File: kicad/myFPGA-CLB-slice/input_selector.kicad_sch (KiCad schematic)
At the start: 26 parts, among them U1 74AHCT595, U32 74LS153, U33 74LS153, U34 74LS153, U35 74LS153

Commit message: fixed kicad names, updated architecure, started CBv
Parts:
- added R12, R13, R14, R15, R16, R17, R18, R19, R21, R23, R25, R27, R29, R31, R33, R35: 100k, Resistor_SMD:R_0805_2012Metric, symbol Device:R
- C?: renamed from C4; Dielectric (none) -> X7R; JLCPCB Part # (none) -> C49678; Part Nr. (none) -> CC0805KRX7R9BB104; Voltage (none) -> 50V
- C?: renamed from C3; Dielectric (none) -> X7R; JLCPCB Part # (none) -> C49678; Part Nr. (none) -> CC0805KRX7R9BB104; Voltage (none) -> 50V
- C?: renamed from C1; Dielectric (none) -> X7R; JLCPCB Part # (none) -> C49678; Part Nr. (none) -> CC0805KRX7R9BB104; Voltage (none) -> 50V
- C?: renamed from C2; Dielectric (none) -> X7R; JLCPCB Part # (none) -> C49678; Part Nr. (none) -> CC0805KRX7R9BB104; Voltage (none) -> 50V
- C?: renamed from C5; Dielectric (none) -> X7R; JLCPCB Part # (none) -> C49678; Part Nr. (none) -> CC0805KRX7R9BB104; Voltage (none) -> 50V
- D10: renamed from D2; value LED -> LED (green); footprint (none) -> LED_SMD:LED_0805_2012Metric; JLCPCB Part # (none) -> C2297; Part Nr. (none) -> C2297
- D11: renamed from D3; value LED -> LED (green); footprint (none) -> LED_SMD:LED_0805_2012Metric; JLCPCB Part # (none) -> C2297; Part Nr. (none) -> C2297
- D12: renamed from D4; value LED -> LED (green); footprint (none) -> LED_SMD:LED_0805_2012Metric; JLCPCB Part # (none) -> C2297; Part Nr. (none) -> C2297
- D13: renamed from D5; value LED -> LED (green); footprint (none) -> LED_SMD:LED_0805_2012Metric; JLCPCB Part # (none) -> C2297; Part Nr. (none) -> C2297
- D14: renamed from D6; value LED -> LED (green); footprint (none) -> LED_SMD:LED_0805_2012Metric; JLCPCB Part # (none) -> C2297; Part Nr. (none) -> C2297
- D15: renamed from D7; value LED -> LED (green); footprint (none) -> LED_SMD:LED_0805_2012Metric; JLCPCB Part # (none) -> C2297; Part Nr. (none) -> C2297
- D16: renamed from D8; value LED -> LED (green); footprint (none) -> LED_SMD:LED_0805_2012Metric; JLCPCB Part # (none) -> C2297; Part Nr. (none) -> C2297
- D9: renamed from D1; value LED -> LED (green); footprint (none) -> LED_SMD:LED_0805_2012Metric; JLCPCB Part # (none) -> C2297; Part Nr. (none) -> C2297
- R20: renamed from R1; footprint (none) -> Resistor_SMD:R_0805_2012Metric; JLCPCB Part # (none) -> C17630; Part Nr. (none) -> 0805W8F3300T5E
- R22: renamed from R2; footprint (none) -> Resistor_SMD:R_0805_2012Metric; JLCPCB Part # (none) -> C17630; Part Nr. (none) -> 0805W8F3300T5E
- R24: renamed from R3; footprint (none) -> Resistor_SMD:R_0805_2012Metric; JLCPCB Part # (none) -> C17630; Part Nr. (none) -> 0805W8F3300T5E
- R26: renamed from R4; footprint (none) -> Resistor_SMD:R_0805_2012Metric; JLCPCB Part # (none) -> C17630; Part Nr. (none) -> 0805W8F3300T5E
- R28: renamed from R5; footprint (none) -> Resistor_SMD:R_0805_2012Metric; JLCPCB Part # (none) -> C17630; Part Nr. (none) -> 0805W8F3300T5E
- R30: renamed from R6; footprint (none) -> Resistor_SMD:R_0805_2012Metric; JLCPCB Part # (none) -> C17630; Part Nr. (none) -> 0805W8F3300T5E
- R32: renamed from R7; footprint (none) -> Resistor_SMD:R_0805_2012Metric; JLCPCB Part # (none) -> C17630; Part Nr. (none) -> 0805W8F3300T5E
- R34: renamed from R8; footprint (none) -> Resistor_SMD:R_0805_2012Metric; JLCPCB Part # (none) -> C17630; Part Nr. (none) -> 0805W8F3300T5E
- renumbered U32 to U34, U33 to U35, U34 to U36, U35 to U37, U1 to U?
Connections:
- net +3V3: no longer C?.1, U?.16 (VCC)
- net CBW_0: no longer U34.11 (I1b), U35.11 (I1b), U36.11 (I1b), U37.11 (I1b)
- net CBW_1: no longer U34.5 (I1a), U35.5 (I1a), U36.5 (I1a), U37.5 (I1a)
- net GND: now also R12.2, R13.2, R14.2, R15.2, R16.2, R17.2, R18.2, R19.2, R21.2, R23.2, R25.2, R27.2, R29.2, R31.2, R33.2, R35.2
- net LA_I0: now also R18.1
- net LA_I1: now also R19.1
- net LB_I0: now also R16.1
- net LB_I1: now also R17.1
- net LC_I0: now also R14.1
- net LC_I1: now also R15.1
- net LD_I0: now also R12.1
- net LD_I1: now also R13.1
- net insel_a_0: now also R21.1
- net insel_a_1: now also R23.1
- net insel_b_0: now also R25.1
- net insel_b_1: now also R27.1
- net insel_c_0: now also R29.1
- net insel_c_1: now also R31.1
- net insel_d_0: now also R33.1
- net insel_d_1: now also R35.1
- new net +3.3VP: C?.1, U?.16 (VCC)
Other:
- moved on the sheet: U34, U35, U36, U37

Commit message: kicad -> pcb started
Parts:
- C? (x5): footprint Capacitor_SMD:C_0805_2012Metric -> Capacitor_SMD:C_0603_1608Metric; Dielectric X7R -> (none); JLCPCB Part # C49678 -> (none); Part Nr. CC0805KRX7R9BB104 -> (none); Voltage 50V -> (none)
- R20: renamed from R12; footprint Resistor_SMD:R_0805_2012Metric -> Resistor_SMD:R_0603_1608Metric; JLCPCB Part # C149504 -> (none); Part Nr. 0805W8F1003T5E -> (none)
- R21: renamed from R13; footprint Resistor_SMD:R_0805_2012Metric -> Resistor_SMD:R_0603_1608Metric; JLCPCB Part # C149504 -> (none); Part Nr. 0805W8F1003T5E -> (none)
- R22: renamed from R14; footprint Resistor_SMD:R_0805_2012Metric -> Resistor_SMD:R_0603_1608Metric; JLCPCB Part # C149504 -> (none); Part Nr. 0805W8F1003T5E -> (none)
- R23: renamed from R15; footprint Resistor_SMD:R_0805_2012Metric -> Resistor_SMD:R_0603_1608Metric; JLCPCB Part # C149504 -> (none); Part Nr. 0805W8F1003T5E -> (none)
- R24: renamed from R16; footprint Resistor_SMD:R_0805_2012Metric -> Resistor_SMD:R_0603_1608Metric; JLCPCB Part # C149504 -> (none); Part Nr. 0805W8F1003T5E -> (none)
- R25: renamed from R17; footprint Resistor_SMD:R_0805_2012Metric -> Resistor_SMD:R_0603_1608Metric; JLCPCB Part # C149504 -> (none); Part Nr. 0805W8F1003T5E -> (none)
- R26: renamed from R18; footprint Resistor_SMD:R_0805_2012Metric -> Resistor_SMD:R_0603_1608Metric; JLCPCB Part # C149504 -> (none); Part Nr. 0805W8F1003T5E -> (none)
- R27: renamed from R19; footprint Resistor_SMD:R_0805_2012Metric -> Resistor_SMD:R_0603_1608Metric; JLCPCB Part # C149504 -> (none); Part Nr. 0805W8F1003T5E -> (none)
- R28: renamed from R20; footprint Resistor_SMD:R_0805_2012Metric -> Resistor_SMD:R_0603_1608Metric; JLCPCB Part # C17630 -> (none); Part Nr. 0805W8F3300T5E -> (none)
- R29: renamed from R21; footprint Resistor_SMD:R_0805_2012Metric -> Resistor_SMD:R_0603_1608Metric; JLCPCB Part # C149504 -> (none); Part Nr. 0805W8F1003T5E -> (none)
- R30: renamed from R22; footprint Resistor_SMD:R_0805_2012Metric -> Resistor_SMD:R_0603_1608Metric; JLCPCB Part # C17630 -> (none); Part Nr. 0805W8F3300T5E -> (none)
- R31: renamed from R23; footprint Resistor_SMD:R_0805_2012Metric -> Resistor_SMD:R_0603_1608Metric; JLCPCB Part # C149504 -> (none); Part Nr. 0805W8F1003T5E -> (none)
- R32: renamed from R24; footprint Resistor_SMD:R_0805_2012Metric -> Resistor_SMD:R_0603_1608Metric; JLCPCB Part # C17630 -> (none); Part Nr. 0805W8F3300T5E -> (none)
- R33: renamed from R25; footprint Resistor_SMD:R_0805_2012Metric -> Resistor_SMD:R_0603_1608Metric; JLCPCB Part # C149504 -> (none); Part Nr. 0805W8F1003T5E -> (none)
- R34: renamed from R26; footprint Resistor_SMD:R_0805_2012Metric -> Resistor_SMD:R_0603_1608Metric; JLCPCB Part # C17630 -> (none); Part Nr. 0805W8F3300T5E -> (none)
- R35: renamed from R27; footprint Resistor_SMD:R_0805_2012Metric -> Resistor_SMD:R_0603_1608Metric; JLCPCB Part # C149504 -> (none); Part Nr. 0805W8F1003T5E -> (none)
- R36: renamed from R28; footprint Resistor_SMD:R_0805_2012Metric -> Resistor_SMD:R_0603_1608Metric; JLCPCB Part # C17630 -> (none); Part Nr. 0805W8F3300T5E -> (none)
- R37: renamed from R29; footprint Resistor_SMD:R_0805_2012Metric -> Resistor_SMD:R_0603_1608Metric; JLCPCB Part # C149504 -> (none); Part Nr. 0805W8F1003T5E -> (none)
- R38: renamed from R30; footprint Resistor_SMD:R_0805_2012Metric -> Resistor_SMD:R_0603_1608Metric; JLCPCB Part # C17630 -> (none); Part Nr. 0805W8F3300T5E -> (none)
- R39: renamed from R31; footprint Resistor_SMD:R_0805_2012Metric -> Resistor_SMD:R_0603_1608Metric; JLCPCB Part # C149504 -> (none); Part Nr. 0805W8F1003T5E -> (none)
- R40: renamed from R32; footprint Resistor_SMD:R_0805_2012Metric -> Resistor_SMD:R_0603_1608Metric; JLCPCB Part # C17630 -> (none); Part Nr. 0805W8F3300T5E -> (none)
- R41: renamed from R33; footprint Resistor_SMD:R_0805_2012Metric -> Resistor_SMD:R_0603_1608Metric; JLCPCB Part # C149504 -> (none); Part Nr. 0805W8F1003T5E -> (none)
- R42: renamed from R34; footprint Resistor_SMD:R_0805_2012Metric -> Resistor_SMD:R_0603_1608Metric; JLCPCB Part # C17630 -> (none); Part Nr. 0805W8F3300T5E -> (none)
- R43: renamed from R35; footprint Resistor_SMD:R_0805_2012Metric -> Resistor_SMD:R_0603_1608Metric; JLCPCB Part # C149504 -> (none); Part Nr. 0805W8F1003T5E -> (none)
- renumbered D9 to D17, D10 to D18, D11 to D19, D12 to D20, D13 to D21, D14 to D22, D15 to D23, D16 to D24

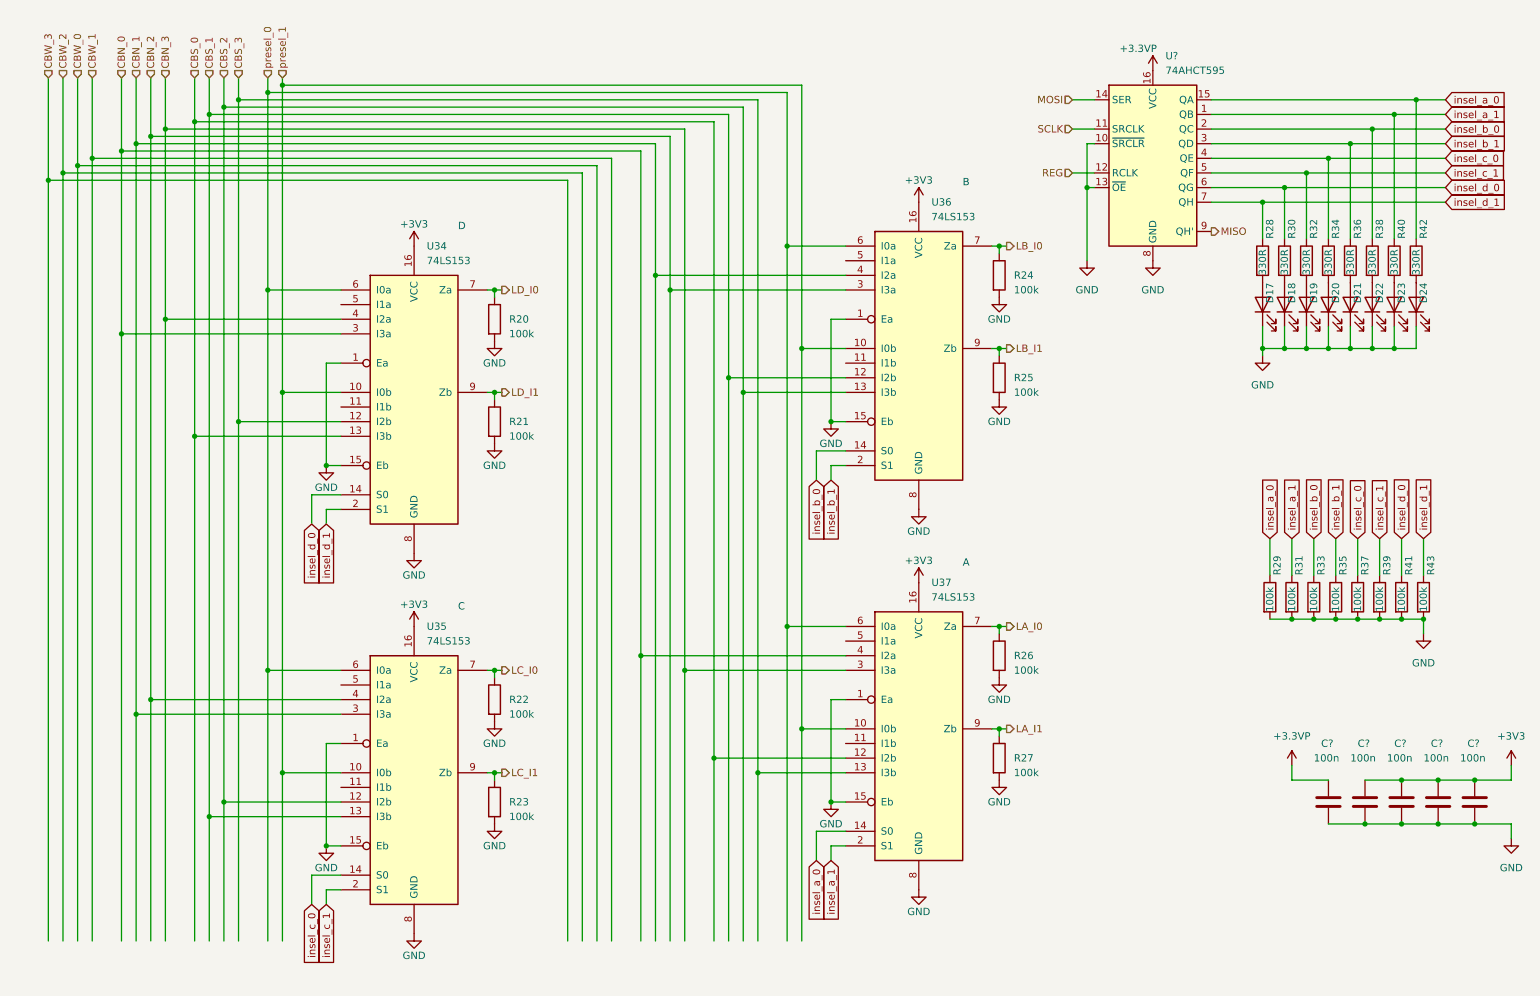
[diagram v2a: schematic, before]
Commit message: kicad: picked JLC parts, fixed routing to match VHDL, started layouting
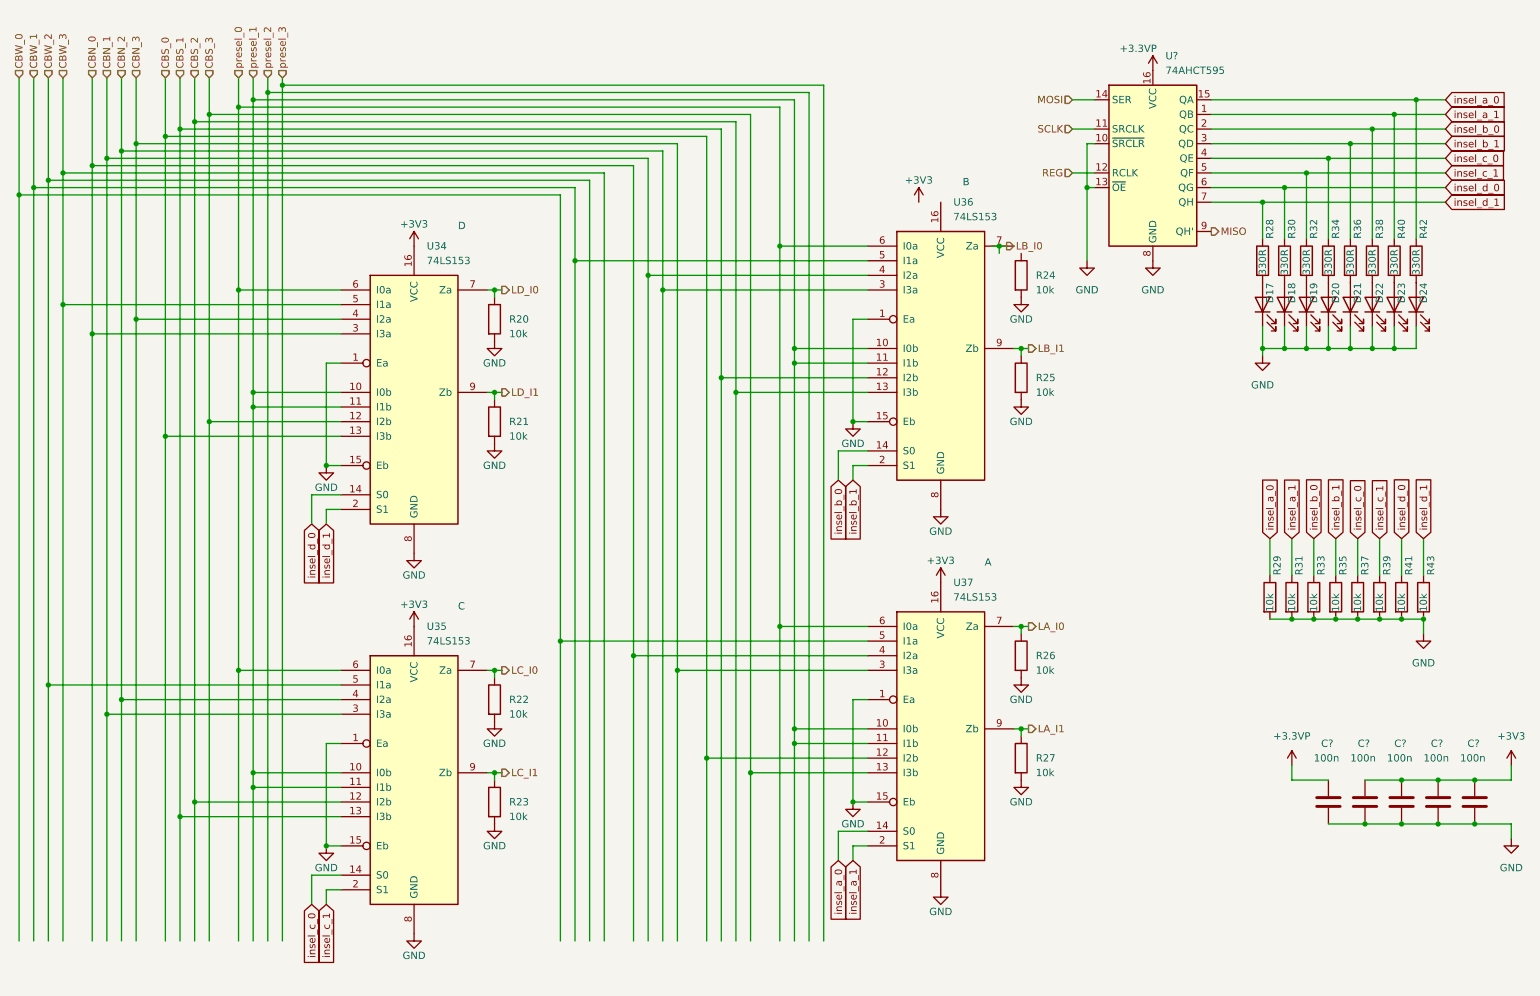
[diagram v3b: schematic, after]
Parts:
- C? (x5): Dielectric (none) -> X7R; JLCPCB Part # (none) -> C14663; Part Nr. (none) -> CC0603KRX7R9BB104; Voltage (none) -> 50
- R20, R21, R22, R23, R24, R25, R26, R27, R29, R31, R33, R35, R37, R39, R41, R43: value 100k -> 10k; JLCPCB Part # (none) -> C25804; Part Nr. (none) -> 0603WAF1002T5E
- R28, R30, R32, R34, R36, R38, R40, R42: JLCPCB Part # (none) -> C23138; Part Nr. (none) -> 0603WAF3300T5E
- U34, U35, U36, U37: footprint Package_SO:SOIC-16_3.9x9.9mm_P1.27mm -> Package_SO:TSSOP-16_4.4x5mm_P0.65mm; JLCPCB Alt # (none) -> C53334 / 74HC153D / SOIC-16-3.9; JLCPCB Part # C53334 -> C150159; package (none) -> TSSOP-16-4.4
- U?: JLCPCB Alt # (none) -> C431479 / 74HC595D / SOIC-16-3.9; package (none) -> SOIC-16-3.9
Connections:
- net +3V3: no longer U36.16 (VCC)
- net CBW_0: now also U37.5 (I1a)
- net CBW_1: now also U36.5 (I1a)
- net CBW_2: now also U35.5 (I1a)
- net CBW_3: now also U34.5 (I1a)
- net LB_I0: no longer R24.1, U36.7 (Za)
- net presel_1: now also U34.11 (I1b), U35.11 (I1b), U36.11 (I1b), U37.11 (I1b)
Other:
- moved on the sheet: R24, R25, R26, R27, U36, U37

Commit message: restart PCB layout
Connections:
- net +3V3: now also U36.16 (VCC)
- net LB_I0: now also R24.1
- net REG renamed LATCH
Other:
- moved on the sheet: R24
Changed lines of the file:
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@@
     (effects (font (size 1.27 1.27)) (justify left))
   )
-  (hierarchical_label "REG" (shape input) (at 199.39 39.37 180) (fields_autoplaced)
+  (hierarchical_label "LATCH" (shape input) (at 199.39 39.37 180) (fields_autoplaced)
     (effects (font (size 1.27 1.27)) (justify right))
   )
@@
     )
   )
-  (symbol (lib_id "Device:R") (at 190.5 57.15 0) (unit 1)
-    (in_bom yes) (on_board yes) (dnp no)
-    (property "Reference" "R24" (at 193.04 57.15 0)
-      (effects (font (size 1.27 1.27)) (justify left))
-    )
-    (property "Value" "10k" (at 193.04 59.69 0)
-      (effects (font (size 1.27 1.27)) (justify left))
-    )
-    (property "Footprint" "Resistor_SMD:R_0603_1608Metric" (at 188.722 57.15 90)
-      (effects (font (size 1.27 1.27)) hide)
-    )
-    (property "Datasheet" "~" (at 190.5 57.15 0)
-      (effects (font (size 1.27 1.27)) hide)
-    )
-    (property "JLCPCB Part #" "C25804" (at 190.5 57.15 0)
-      (effects (font (size 1.27 1.27)) hide)
-    )
-    (property "Part Nr." "0603WAF1002T5E" (at 190.5 57.15 0)
-      (effects (font (size 1.27 1.27)) hide)
-    )
-    (property "Dielectric" "" (at 190.5 57.15 0)
-      (effects (font (size 1.27 1.27)) hide)
-    )
-    (property "Voltage" "" (at 190.5 57.15 0)
-      (effects (font (size 1.27 1.27)) hide)
-    )
-    (property "JLCPCB Alt #" "" (at 190.5 57.15 0)
-      (effects (font (size 1.27 1.27)) hide)
-    )
-    (property "package" "" (at 190.5 57.15 0)
+  (symbol (lib_id "Device:R") (at 186.69 57.15 0) (unit 1)
+    (in_bom yes) (on_board yes) (dnp no)
+    (property "Reference" "R24" (at 189.23 57.15 0)
+      (effects (font (size 1.27 1.27)) (justify left))
+    )
+    (property "Value" "10k" (at 189.23 59.69 0)
+      (effects (font (size 1.27 1.27)) (justify left))
+    )
+    (property "Footprint" "Resistor_SMD:R_0603_1608Metric" (at 184.912 57.15 90)
+      (effects (font (size 1.27 1.27)) hide)
+    )
+    (property "Datasheet" "~" (at 186.69 57.15 0)
+      (effects (font (size 1.27 1.27)) hide)
+    )
+    (property "JLCPCB Part #" "C25804" (at 186.69 57.15 0)
+      (effects (font (size 1.27 1.27)) hide)
+    )
+    (property "Part Nr." "0603WAF1002T5E" (at 186.69 57.15 0)
+      (effects (font (size 1.27 1.27)) hide)
+    )
+    (property "Dielectric" "" (at 186.69 57.15 0)
+      (effects (font (size 1.27 1.27)) hide)
+    )
+    (property "Voltage" "" (at 186.69 57.15 0)
+      (effects (font (size 1.27 1.27)) hide)
+    )
+    (property "JLCPCB Alt #" "" (at 186.69 57.15 0)
+      (effects (font (size 1.27 1.27)) hide)
+    )
+    (property "package" "" (at 186.69 57.15 0)
       (effects (font (size 1.27 1.27)) hide)
     )
@@
     )
   )
-  (symbol (lib_id "power:GND") (at 190.5 60.96 0) (unit 1)
-    (in_bom yes) (on_board yes) (dnp no)
-    (property "Reference" "#PWR?" (at 190.5 67.31 0)
-      (effects (font (size 1.27 1.27)) hide)
-    )
-    (property "Value" "GND" (at 190.5 64.77 0)
+  (symbol (lib_id "power:GND") (at 186.69 60.96 0) (unit 1)
+    (in_bom yes) (on_board yes) (dnp no)
+    (property "Reference" "#PWR?" (at 186.69 67.31 0)
+      (effects (font (size 1.27 1.27)) hide)
+    )
+    (property "Value" "GND" (at 186.69 64.77 0)
       (effects (font (size 1.27 1.27)))
     )
-    (property "Footprint" "" (at 190.5 60.96 0)
-      (effects (font (size 1.27 1.27)) hide)
-    )
-    (property "Datasheet" "" (at 190.5 60.96 0)
+    (property "Footprint" "" (at 186.69 60.96 0)
+      (effects (font (size 1.27 1.27)) hide)
+    )
+    (property "Datasheet" "" (at 186.69 60.96 0)
       (effects (font (size 1.27 1.27)) hide)
     )
@@
     )
   )
-  (symbol (lib_id "power:+3V3") (at 172.72 44.45 0) (unit 1)
-    (in_bom yes) (on_board yes) (dnp no)
-    (property "Reference" "#PWR?" (at 172.72 48.26 0)
-      (effects (font (size 1.27 1.27)) hide)
-    )
-    (property "Value" "+3V3" (at 172.72 40.64 0)
+  (symbol (lib_id "power:+3V3") (at 176.53 44.45 0) (unit 1)
+    (in_bom yes) (on_board yes) (dnp no)
+    (property "Reference" "#PWR?" (at 176.53 48.26 0)
+      (effects (font (size 1.27 1.27)) hide)
+    )
+    (property "Value" "+3V3" (at 176.53 40.64 0)
       (effects (font (size 1.27 1.27)))
     )
-    (property "Footprint" "" (at 172.72 44.45 0)
-      (effects (font (size 1.27 1.27)) hide)
-    )
-    (property "Datasheet" "" (at 172.72 44.45 0)
-      (effects (font (size 1.27 1.27)) hide)
-    )
+    (property "Footprint" "" (at 176.53 44.45 0)
+      (effects (font (size 1.27 1.27)) hide)
+    )
+    (property "Datasheet" "" (at 176.53 44.45 0)
+      (effects (font (size 1.27 1.27)) hide)
+    )
